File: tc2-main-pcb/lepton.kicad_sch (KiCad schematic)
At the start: 29 parts, among them U10 TD6810, U11 TD6810, U7 ME6216A28XG, U8 Flir_LEPTON, U9 3N25000G33YC

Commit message: P2 milestone
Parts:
- added R35 (x2): 100k, Resistor_SMD:R_0402_1005Metric, symbol Device:R
- added TP28 (x4): TestPoint_2Pole, cacophony-library:test-point-2p, symbol Connector:TestPoint_2Pole
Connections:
- net +1V2: now also TP28.2
- net +2V8: now also TP28.2
- net +3V0: now also R35.1, R35.1, TP28.2
- net +3V3: now also TP28.2
- net GND: now also TP28.1, TP28.1, TP28.1, TP28.1
- net LEPTON_I2C_SCL: now also R35.2
- net LEPTON_I2C_SDA: now also R35.2

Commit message: P3-Nov release
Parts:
- removed TP28 (x4): TestPoint_2Pole, cacophony-library:test-point-2p, symbol Connector:TestPoint_2Pole
- added TP3 (x2), TP5: TP_2P, cacophony-library:test-point-2p, symbol cacophony-library:TestPoint_2Pole
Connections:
- net +1V2: now also TP3.2
- net +2V8: now also TP5.2
- net +3V0: now also TP3.2
- net GND: now also TP3.1, TP3.1, TP5.1
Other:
- moved on the sheet: C21, C23, U7

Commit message: v0.4.0
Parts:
- TP4, TP8: renamed from TP3; now left out of the parts list
- TP5: now left out of the parts list
- U10, U11: footprint Package_TO_SOT_SMD:TSOT-23-5 -> cacophony-library:TSOT-23-5; JLCPCB C16510 -> (none)
- U7: JLCPCB C427601 -> (none)
- U9: JLCPCB C252341 -> (none)
- renumbered C3 to C41, C3 to C42, R35 to R13, R10 to R33, R35 to R36

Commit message: Small update for v0.4.1
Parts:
- L1, L2: LCSC C354574 -> C436646
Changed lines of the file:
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@@
 			)
 		)
-		(property "LCSC" "C354574"
+		(property "LCSC" "C436646"
 			(at 236.22 24.13 0)
 			(effects
@@
 			)
 		)
-		(property "LCSC" "C354574"
+		(property "LCSC" "C436646"
 			(at 236.22 72.39 0)
 			(effects

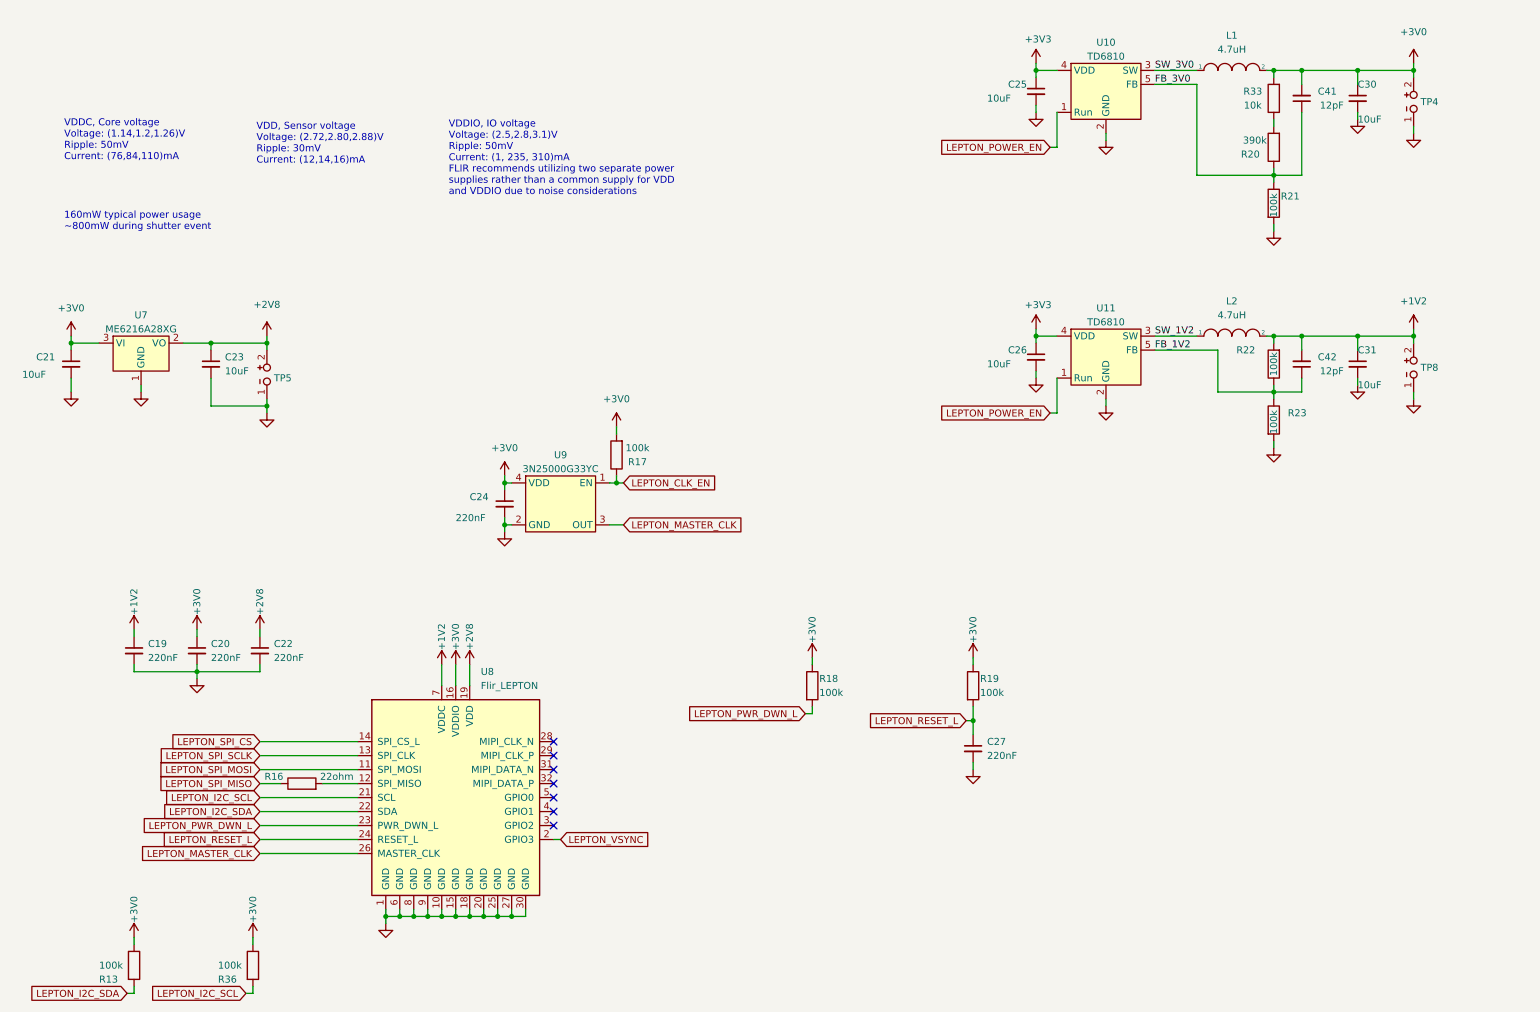
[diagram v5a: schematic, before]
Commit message: Update to use touch sensor
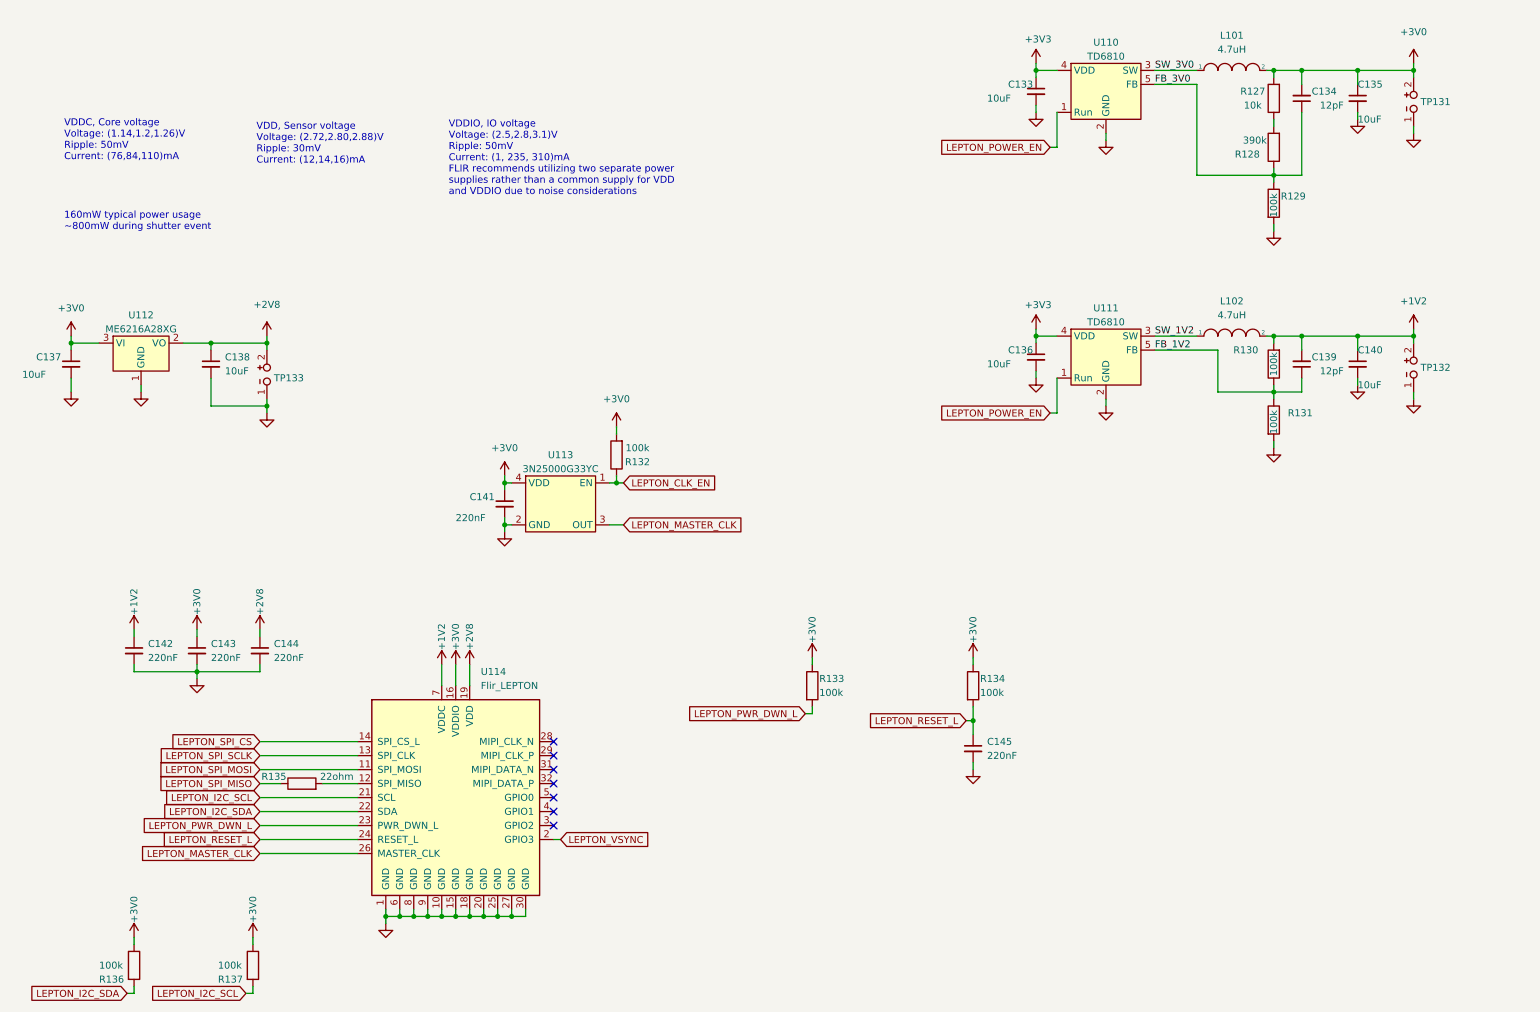
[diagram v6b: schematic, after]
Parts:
- renumbered C25 to C133, C41 to C134, C30 to C135, C26 to C136, C21 to C137, C23 to C138, C42 to C139, C31 to C140, C24 to C141, C19 to C142, C20 to C143, C22 to C144, C27 to C145, L1 to L101, L2 to L102, R33 to R127, R20 to R128, R21 to R129, R22 to R130, R23 to R131, R17 to R132, R18 to R133, R19 to R134, R16 to R135, R13 to R136, R36 to R137, TP4 to TP131, TP8 to TP132, TP5 to TP133, U10 to U110, U11 to U111, U7 to U112, U9 to U113, U8 to U114

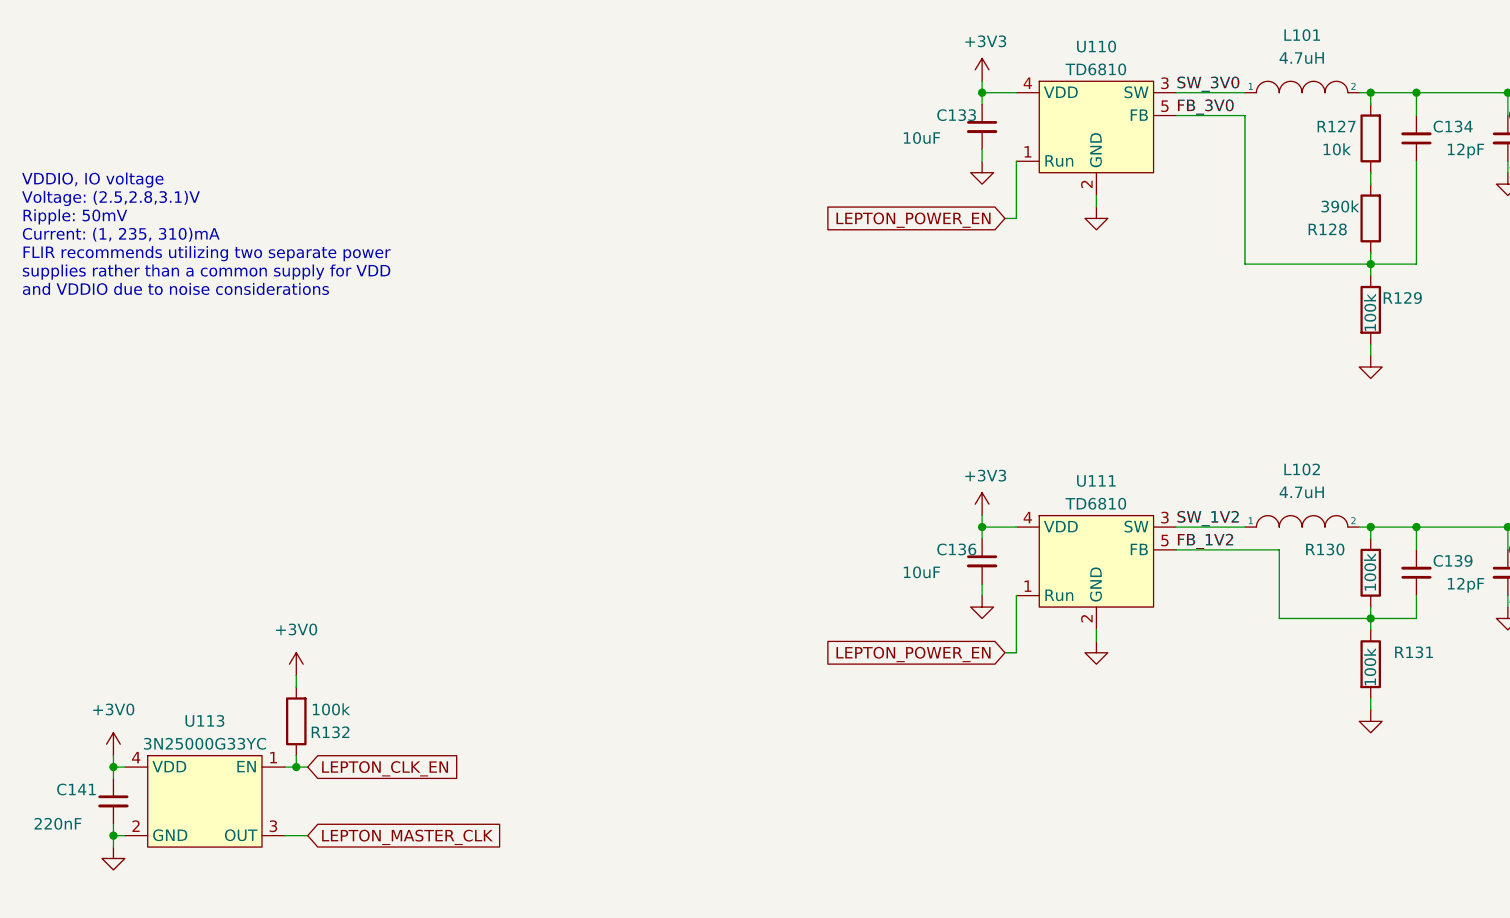
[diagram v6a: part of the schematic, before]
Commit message: Upgraded to new kicad version
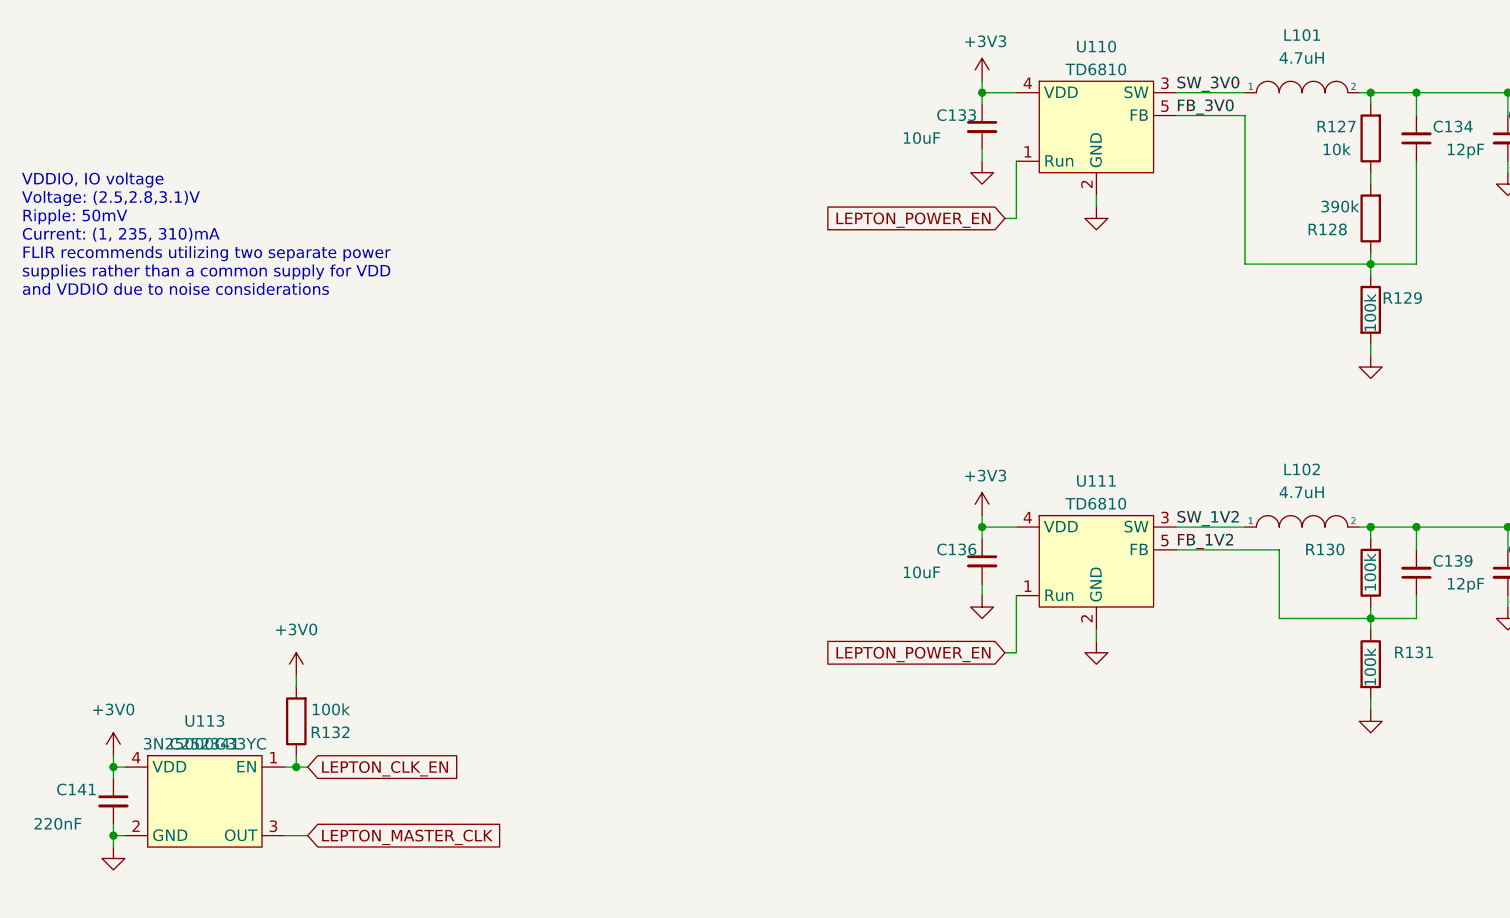
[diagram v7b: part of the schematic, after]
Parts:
- U113: JLCPCB (none) -> C252341; LCSC Part (none) -> C252341
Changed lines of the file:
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@@
 (kicad_sch
-	(version 20231120)
+	(version 20250114)
 	(generator "eeschema")
-	(generator_version "8.0")
+	(generator_version "9.0")
 	(paper "A4")
+	(text "160mW typical power usage\n~800mW during shutter event"
+		(exclude_from_sim no)
+		(at 24.13 53.34 0)
+		(effects
+			(font
+				(size 1.27 1.27)
+			)
+			(justify left bottom)
+		)
+	)
+	(text "VDDC, Core voltage\nVoltage: (1.14,1.2,1.26)V\nRipple: 50mV\nCurrent: (76,84,110)mA"
+		(exclude_from_sim no)
+		(at 24.13 40.64 0)
+		(effects
+			(font
+				(size 1.27 1.27)
+			)
+			(justify left bottom)
+		)
+	)
+	(text "VDD, Sensor voltage\nVoltage: (2.72,2.80,2.88)V\nRipple: 30mV\nCurrent: (12,14,16)mA\n"
+		(exclude_from_sim no)
+		(at 59.055 41.275 0)
+		(effects
+			(font
+				(size 1.27 1.27)
+			)
+			(justify left bottom)
+		)
+	)
+	(text "VDDIO, IO voltage\nVoltage: (2.5,2.8,3.1)V\nRipple: 50mV\nCurrent: (1, 235, 310)mA\nFLIR recommends utilizing two separate power \nsupplies rather than a common supply for VDD \nand VDDIO due to noise considerations\n"
+		(exclude_from_sim no)
+		(at 93.98 46.99 0)
+		(effects
+			(font
+				(size 1.27 1.27)
+			)
+			(justify left bottom)
+		)
+	)
 	(junction
 		(at 269.24 24.13)
@@
 		)
 	)
-	(text "160mW typical power usage\n~800mW during shutter event"
-		(exclude_from_sim no)
-		(at 24.13 53.34 0)
-		(effects
-			(font
-				(size 1.27 1.27)
-			)
-			(justify left bottom)
-		)
-	)
-	(text "VDDC, Core voltage\nVoltage: (1.14,1.2,1.26)V\nRipple: 50mV\nCurrent: (76,84,110)mA"
-		(exclude_from_sim no)
-		(at 24.13 40.64 0)
-		(effects
-			(font
-				(size 1.27 1.27)
-			)
-			(justify left bottom)
-		)
-	)
-	(text "VDD, Sensor voltage\nVoltage: (2.72,2.80,2.88)V\nRipple: 30mV\nCurrent: (12,14,16)mA\n"
-		(exclude_from_sim no)
-		(at 59.055 41.275 0)
-		(effects
-			(font
-				(size 1.27 1.27)
-			)
-			(justify left bottom)
-		)
-	)
-	(text "VDDIO, IO voltage\nVoltage: (2.5,2.8,3.1)V\nRipple: 50mV\nCurrent: (1, 235, 310)mA\nFLIR recommends utilizing two separate power \nsupplies rather than a common supply for VDD \nand VDDIO due to noise considerations\n"
-		(exclude_from_sim no)
-		(at 93.98 46.99 0)
-		(effects
-			(font
-				(size 1.27 1.27)
-			)
-			(justify left bottom)
-		)
-	)
 	(label "FB_3V0"
 		(at 222.25 26.67 0)
-		(fields_autoplaced yes)
 		(effects
 			(font
@@
 	(label "SW_1V2"
 		(at 222.25 72.39 0)
-		(fields_autoplaced yes)
 		(effects
 			(font
@@
 	(label "FB_1V2"
 		(at 222.25 74.93 0)
-		(fields_autoplaced yes)
 		(effects
 			(font
@@
 	(label "SW_3V0"
 		(at 222.25 24.13 0)
-		(fields_autoplaced yes)
 		(effects
 			(font
@@
 			)
 		)
-		(property "JLCPCB" ""
+		(property "JLCPCB" "C252341"
 			(at 114.3 96.52 0)
 			(effects
@@
 			)
 		)
+		(property "LCSC Part" "C252341"
+			(at 114.3 96.52 0)
+			(effects
+				(font
+					(size 1.27 1.27)
+				)
+			)
+		)

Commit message: Tidy up for making an order for v0.7.3
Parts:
- C133, C135, C136, C137, C138, C140: LCSC C19702 -> (none); LCSC Part (none) -> C19702
- C134, C139: LCSC C1547 -> (none); LCSC Part (none) -> C1547
- C141, C142, C143, C144, C145: LCSC C16772 -> (none); LCSC Part (none) -> C16772
- L101, L102: LCSC C436646 -> (none); LCSC Part (none) -> C436646
- R127: LCSC C25744 -> (none); LCSC Part (none) -> C25744
- R128: LCSC C2943536 -> (none); LCSC Part (none) -> C2943536
- R129, R130, R131, R132, R133, R134, R136, R137: LCSC C25741 -> (none); LCSC Part (none) -> C25741
- R135: value 22ohm -> 22Ω; LCSC C25092 -> (none); LCSC Part (none) -> C25092
- U110, U111: LCSC C16510 -> (none); LCSC Part (none) -> C16510
- U112: LCSC C427601 -> (none); LCSC Part (none) -> C427601
- U113: LCSC C252341 -> (none)
- U114: LCSC C585422 -> (none); LCSC Part (none) -> C585422
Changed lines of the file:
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@@
 			)
 		)
-		(property "LCSC" "C25741"
+		(property "LCSC Part" "C25741"
 			(at 160.02 135.89 0)
 			(effects
@@
 			)
 		)
-		(property "LCSC" "C19702"
+		(property "LCSC Part" "C19702"
 			(at 25.4 77.47 0)
 			(effects
@@
 			)
 		)
-		(property "LCSC" "C19702"
+		(property "LCSC Part" "C19702"
 			(at 259.08 77.47 0)
 			(effects
@@
 			)
 		)
-		(property "LCSC" "C16772"
+		(property "LCSC Part" "C16772"
 			(at 48.26 129.54 0)
 			(effects
@@
 			)
 		)
-		(property "LCSC" "C19702"
+		(property "LCSC Part" "C19702"
 			(at 200.66 27.94 0)
 			(effects
@@
 			)
 		)
-		(property "LCSC" "C25741"
+		(property "LCSC Part" "C25741"
 			(at 36.83 186.69 0)
 			(effects
@@
 			)
 		)
-		(property "LCSC" "C25744"
+		(property "LCSC Part" "C25744"
 			(at 243.84 29.21 0)
 			(effects
@@
 			)
 		)
-		(property "LCSC" "C16772"
+		(property "LCSC Part" "C16772"
 			(at 104.14 102.87 0)
 			(effects
@@
 			)
 		)
-		(property "LCSC" "C25741"
+		(property "LCSC Part" "C25741"
 			(at 243.84 77.47 0)
 			(effects
@@
 			)
 		)
-		(property "LCSC" "C25741"
+		(property "LCSC Part" "C25741"
 			(at 58.42 186.69 0)
 			(effects
@@
 			)
 		)
-		(property "LCSC" "C1547"
+		(property "LCSC Part" "C1547"
 			(at 248.92 77.47 0)
 			(effects
@@
 			)
 		)
-		(property "LCSC" "C19702"
+		(property "LCSC Part" "C19702"
 			(at 50.8 77.47 0)
 			(effects
@@
 			)
 		)
-		(property "LCSC" "C25741"
+		(property "LCSC Part" "C25741"
 			(at 189.23 135.89 0)
 			(effects
@@
 			)
 		)
-		(property "LCSC" "C1547"
+		(property "LCSC Part" "C1547"
 			(at 248.92 29.21 0)
 			(effects
@@
 			)
 		)
-		(property "LCSC" "C252341"
+		(property "LCSC Part" "C252341"
 			(at 114.3 96.52 0)
 			(effects
@@
 			)
 		)
-		(property "LCSC" "C25741"
+		(property "LCSC Part" "C25741"
 			(at 243.84 48.26 0)
 			(effects
@@
 			)
 		)
-		(property "LCSC" "C436646"
+		(property "LCSC Part" "C436646"
 			(at 236.22 24.13 0)
 			(effects
@@
 			)
 		)
-		(property "LCSC" "C19702"
+		(property "LCSC Part" "C19702"
 			(at 259.08 29.21 0)
 			(effects
@@
 			)
 		)
-		(property "LCSC" "C16772"
+		(property "LCSC Part" "C16772"
 			(at 59.69 129.54 0)
 			(effects
@@
 			)
 		)
-		(property "LCSC" "C16510"
+		(property "LCSC Part" "C16510"
 			(at 213.36 21.59 0)
 			(effects
@@
 			)
 		)
-		(property "Value" "22ohm"
+		(property "Value" "22Ω"
 			(at 73.66 152.4 90)
 			(effects
@@
 			)
 		)
-		(property "LCSC" "C25092"
+		(property "LCSC Part" "C25092"
 			(at 67.31 153.67 0)
 			(effects
@@
 			)
 		)
-		(property "LCSC" "C585422"
+		(property "LCSC Part" "C585422"
 			(at 95.25 156.21 0)
 			(effects
@@
 			)
 		)
-		(property "LCSC" "C25741"
+		(property "LCSC Part" "C25741"
 			(at 243.84 87.63 0)
 			(effects
@@
 			)
 		)
-		(property "LCSC" "C16772"
+		(property "LCSC Part" "C16772"
 			(at 189.23 147.32 0)
 			(effects
@@
 			)
 		)
-		(property "LCSC" "C436646"
+		(property "LCSC Part" "C436646"
 			(at 236.22 72.39 0)
 			(effects
@@
 			)
 		)
-		(property "LCSC" "C16772"
+		(property "LCSC Part" "C16772"
 			(at 36.83 129.54 0)
 			(effects
@@
 			)
 		)
-		(property "LCSC" "C19702"
+		(property "LCSC Part" "C19702"
 			(at 200.66 76.2 0)
 			(effects
@@
 			)
 		)
-		(property "LCSC" "C16510"
+		(property "LCSC Part" "C16510"
 			(at 213.36 69.85 0)
 			(effects
@@
 			)
 		)
-		(property "LCSC" "C2943536"
+		(property "LCSC Part" "C2943536"
 			(at 243.84 38.1 0)
 			(effects
@@
 			)
 		)
-		(property "LCSC" "C25741"
+		(property "LCSC Part" "C25741"
 			(at 124.46 93.98 0)
 			(effects
@@
 			)
 		)
-		(property "LCSC" "C427601"
+		(property "LCSC Part" "C427601"
 			(at 38.1 66.04 0)
 			(effects
